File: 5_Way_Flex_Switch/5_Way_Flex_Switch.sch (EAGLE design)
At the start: 9 parts

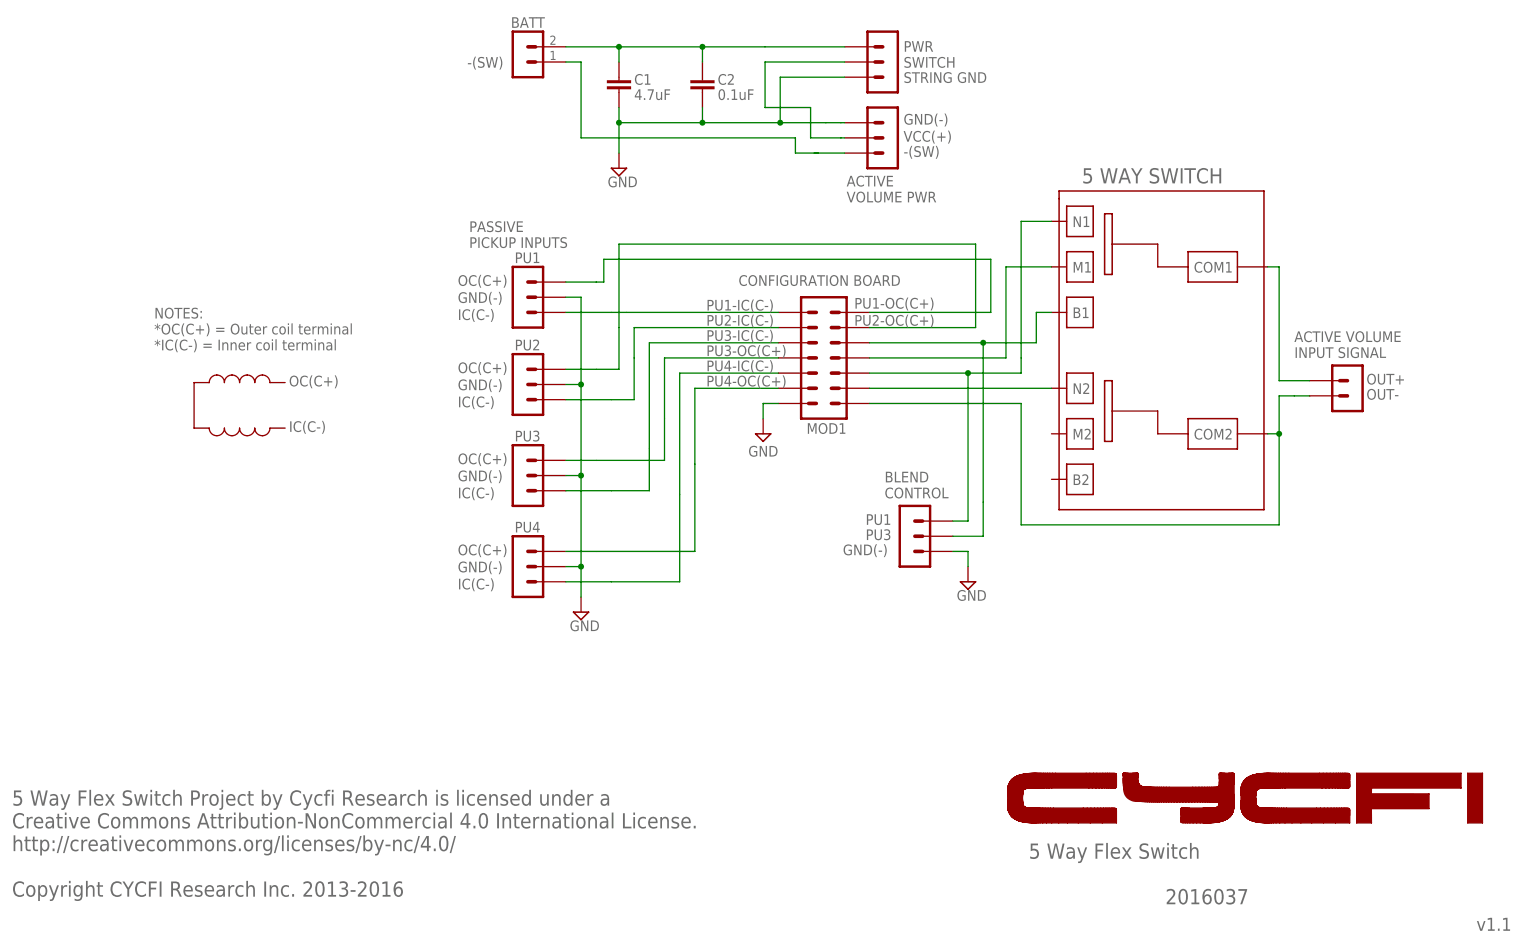
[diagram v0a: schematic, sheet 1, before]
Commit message: Updates/ label modifications to make them consistent
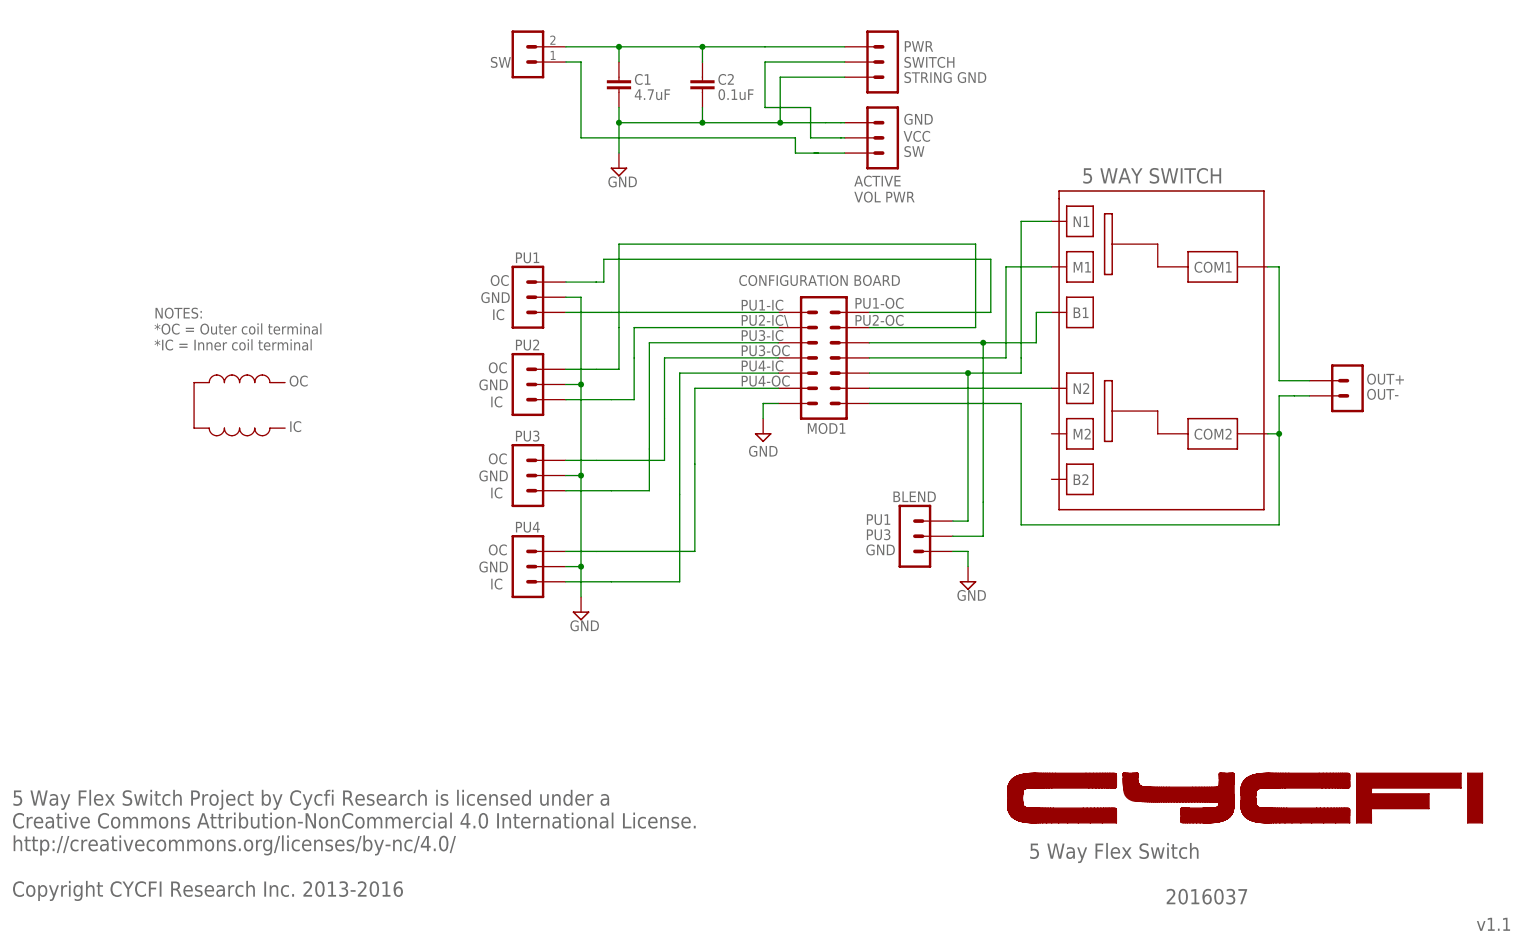
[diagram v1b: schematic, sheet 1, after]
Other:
- note added: "ACTIVE VOL PWR"
- note added: "BLEND"
- note added: "GND"
- note added: "IC"
- note added: "NOTES: *OC = Outer coil terminal *IC = Inner coil terminal"
- note added: "OC"
- note added: "PU1-IC"
- note added: "PU1-OC"
- note added: "PU2-IC\"
- note added: "PU2-OC"
- note added: "PU3-IC"
- note added: "PU3-OC"
- note added: "PU4-IC"
- note added: "PU4-OC"
- note added: "SW"
- note added: "VCC"
- note removed: "-(SW)"
- note removed: "ACTIVE VOLUME INPUT SIGNAL"
- note removed: "ACTIVE VOLUME PWR"
- note removed: "BATT"
- note removed: "BLEND CONTROL"
- note removed: "GND(-)"
- note removed: "IC(C-)"
- note removed: "NOTES: *OC(C+) = Outer coil terminal *IC(C-) = Inner coil terminal"
- note removed: "OC(C+)"
- note removed: "PASSIVE PICKUP INPUTS"
- note removed: "PU1-IC(C-)"
- note removed: "PU1-OC(C+)"
- note removed: "PU2-IC(C-)"
- note removed: "PU2-OC(C+)"
- note removed: "PU3-IC(C-)"
- note removed: "PU3-OC(C+)"
- note removed: "PU4-IC(C-)"
- note removed: "PU4-OC(C+)"
- note removed: "VCC(+)"

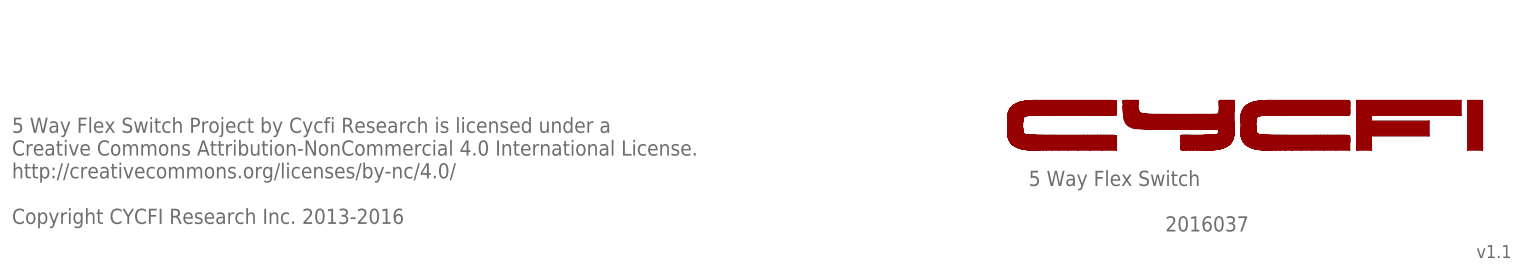
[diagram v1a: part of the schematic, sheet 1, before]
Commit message: Updated schematic licenses
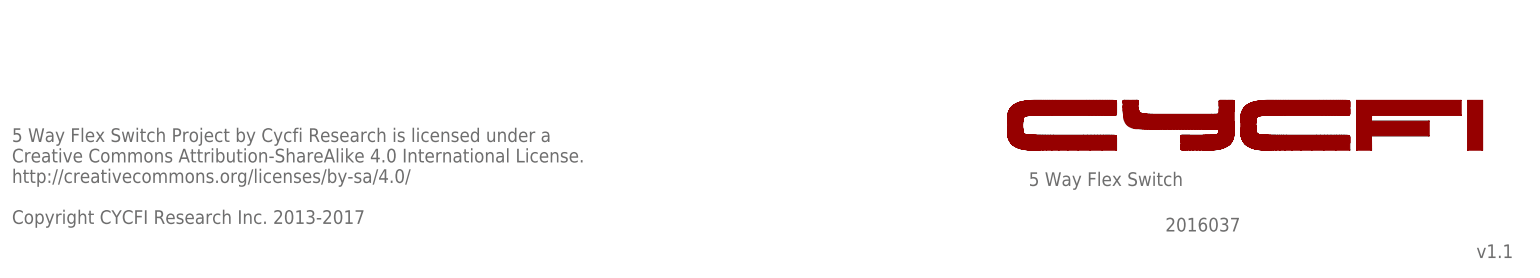
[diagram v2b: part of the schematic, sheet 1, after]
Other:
- note added: "5 Way Flex Switch Project by Cycfi Research is licensed under a Creative Commons Attribution-ShareAlike 4.0 International License. http://creativecommons.org/licenses/by-sa/4.0/ Copyright CYCFI Research Inc. 2013-2017"
- note removed: "5 Way Flex Switch Project by Cycfi Research is licensed under a Creative Commons Attribution-NonCommercial 4.0 International License. http://creativecommons.org/licenses/by-nc/4.0/ Copyright CYCFI Research Inc. 2013-2016"
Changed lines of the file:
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@@
 <text x="53.975" y="90.4875" size="1.778" layer="95">IC</text>
 <text x="53.975" y="98.1075" size="1.778" layer="95">OC</text>
-<text x="177.8" y="19.05" size="2.54" layer="95">5 Way Flex Switch</text>
-<text x="252.73" y="6.985" size="2.1844" layer="95">v1.1</text>
-<text x="7.62" y="12.7" size="2.54" layer="95">5 Way Flex Switch Project by Cycfi Research is licensed under a
-Creative Commons Attribution-NonCommercial 4.0 International License.
-http://creativecommons.org/licenses/by-nc/4.0/
-Copyright CYCFI Research Inc. 2013-2016</text>
-<text x="200.66" y="11.43" size="2.54" layer="95">2016037</text>
+<text x="177.8" y="19.05" size="2.286" layer="95">5 Way Flex Switch</text>
+<text x="252.73" y="6.985" size="2.286" layer="95">v1.1</text>
+<text x="7.62" y="12.7" size="2.286" layer="95">5 Way Flex Switch Project by Cycfi Research is licensed under a
+Creative Commons Attribution-ShareAlike 4.0 International License.
+http://creativecommons.org/licenses/by-sa/4.0/
+Copyright CYCFI Research Inc. 2013-2017</text>
+<text x="200.66" y="11.43" size="2.286" layer="95">2016037</text>
 <wire x1="192.47528125" y1="25.047221875" x2="190.115640625" y2="25.047221875" width="0" layer="94"/>
 <wire x1="190.115640625" y1="25.047221875" x2="188.10833125" y2="25.047225" width="0" layer="94"/>
@@
 <instance part="FRAME1" gate="G$1" x="0" y="0"/>
 <instance part="FRAME1" gate="G$2" x="162.56" y="0" smashed="yes">
-<attribute name="LAST_DATE_TIME" x="175.26" y="1.27" size="2.54" layer="94" font="vector"/>
-<attribute name="SHEET" x="248.92" y="1.27" size="2.54" layer="94" font="vector"/>
+<attribute name="LAST_DATE_TIME" x="175.26" y="1.27" size="2.54" layer="94"/>
+<attribute name="SHEET" x="248.92" y="1.27" size="2.54" layer="94"/>
 </instance>
 </instances>
@@
 <text x="86.36" y="111.125" size="1.778" layer="95">GND</text>
 <text x="101.2825" y="117.7925" size="1.778" layer="95">H1</text>
-<text x="177.8" y="19.05" size="2.54" layer="95">5 Way Flex Switch</text>
-<text x="252.73" y="6.985" size="2.1844" layer="95">v1.1</text>
-<text x="7.62" y="12.7" size="2.54" layer="95">5 Way Flex Switch Project by Cycfi Research is licensed under a
-Creative Commons Attribution-NonCommercial 4.0 International License.
-http://creativecommons.org/licenses/by-nc/4.0/
-Copyright CYCFI Research Inc. 2013-2016</text>
-<text x="200.66" y="11.43" size="2.54" layer="95">2016037</text>
+<text x="177.8" y="19.05" size="2.286" layer="95">5 Way Flex Switch</text>
+<text x="252.73" y="6.985" size="2.286" layer="95">v1.1</text>
+<text x="7.62" y="12.7" size="2.286" layer="95">5 Way Flex Switch Project by Cycfi Research is licensed under a
+Creative Commons Attribution-ShareAlike 4.0 International License.
+http://creativecommons.org/licenses/by-sa/4.0/
+Copyright CYCFI Research Inc. 2013-2017</text>
+<text x="200.66" y="11.43" size="2.286" layer="95">2016037</text>
 <wire x1="192.47528125" y1="25.047221875" x2="190.115640625" y2="25.047221875" width="0" layer="94"/>
 <wire x1="190.115640625" y1="25.047221875" x2="188.10833125" y2="25.047225" width="0" layer="94"/>
